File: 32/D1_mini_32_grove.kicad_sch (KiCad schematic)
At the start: 3 parts, among them J1 Conn_01x04_Pin, J2 Conn_01x04_Pin, U1 esp32-wemos-d1-mini

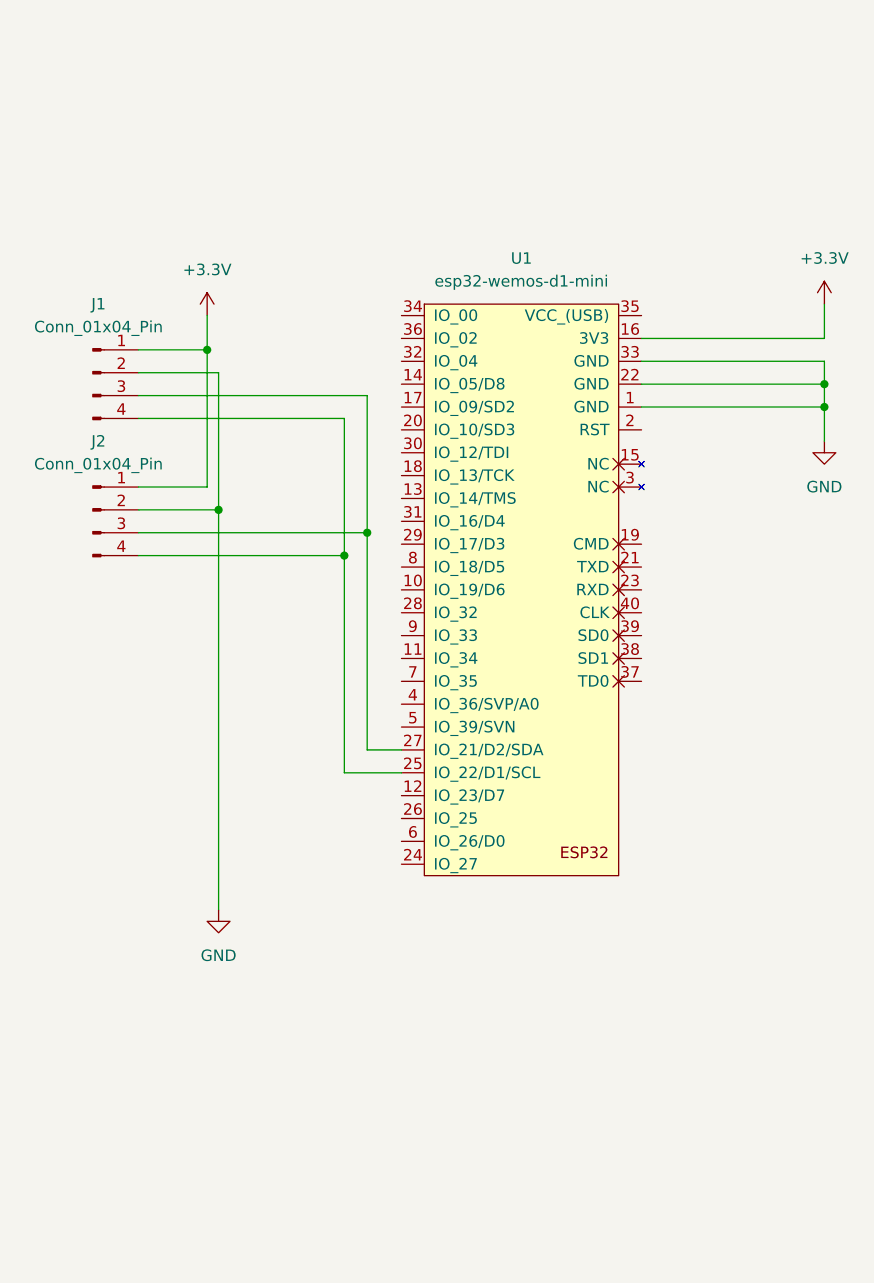
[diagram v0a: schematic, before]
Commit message: First draft of 32 board ready for testrun
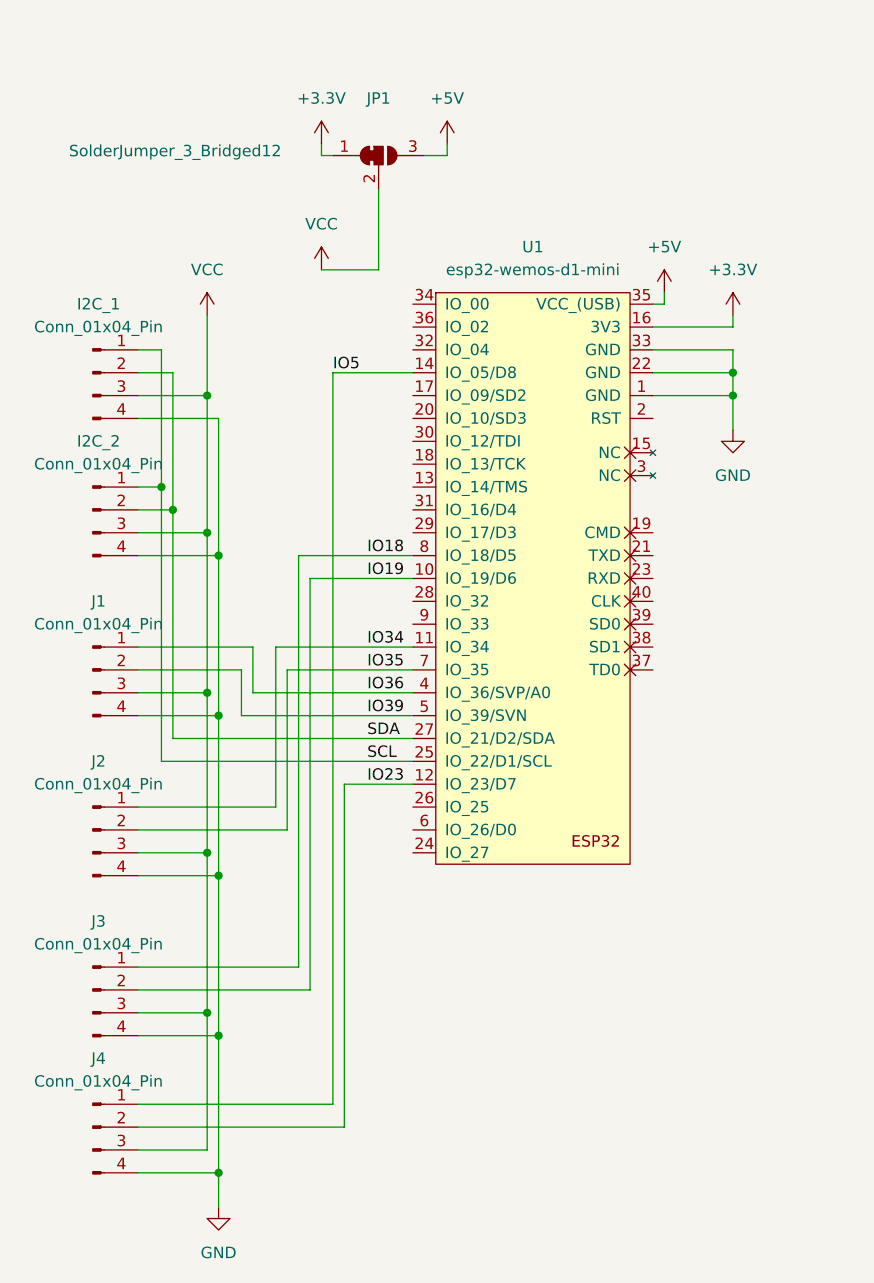
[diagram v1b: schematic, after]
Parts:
- added J1, J2, J3, J4: Conn_01x04_Pin, pretty:NS-Tech_Grove_1x04_P2mm_Vertical, symbol Connector:Conn_01x04_Pin
- added JP1: SolderJumper_3_Bridged12, Jumper:SolderJumper-3_P1.3mm_Bridged12_RoundedPad1.0x1.5mm_NumberLabels, symbol Jumper:SolderJumper_3_Bridged12
- renumbered J1 to I2C_1, J2 to I2C_2
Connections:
- net +3.3V: now also JP1.1 (A); no longer I2C_1.1 (Pin_1), I2C_2.1 (Pin_1)
- net GND: now also I2C_1.4 (Pin_4), I2C_2.4 (Pin_4), J1.4 (Pin_4), J2.4 (Pin_4), J3.4 (Pin_4), J4.4 (Pin_4); no longer I2C_1.2 (Pin_2), I2C_2.2 (Pin_2)
- net IO19: now reaches U1.10 (IO_19/D6)
- net IO19: now also J3.2 (Pin_2)
- net IO34: now reaches U1.11 (IO_34)
- net IO34: now also J2.1 (Pin_1)
- net IO23: now reaches U1.12 (IO_23/D7)
- net IO23: now also J4.2 (Pin_2)
- net IO5: now reaches U1.14 (IO_05/D8)
- net IO5: now also J4.1 (Pin_1)
- net VCC: now reaches I2C_1.3 (Pin_3), I2C_2.3 (Pin_3)
- net VCC: now also J1.3 (Pin_3), J2.3 (Pin_3), J3.3 (Pin_3), J4.3 (Pin_3), JP1.2 (C); no longer U1.27 (IO_21/D2/SDA)
- net +5V: now reaches U1.35 (VCC_(USB))
- net +5V: now also JP1.3 (B)
- net IO36: now reaches U1.4 (IO_36/SVP/A0)
- net IO36: now also J1.1 (Pin_1)
- net IO39: now reaches U1.5 (IO_39/SVN)
- net IO39: now also J1.2 (Pin_2)
- net IO35: now reaches U1.7 (IO_35)
- net IO35: now also J2.2 (Pin_2)
- net IO18: now reaches U1.8 (IO_18/D5)
- net IO18: now also J3.1 (Pin_1)
- new net SCL: I2C_1.1 (Pin_1), I2C_2.1 (Pin_1), U1.25 (IO_22/D1/SCL)
- new net SDA: I2C_1.2 (Pin_2), I2C_2.2 (Pin_2), U1.27 (IO_21/D2/SDA)
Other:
- moved on the sheet: U1

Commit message: Added a switch for VCC selector instead of solder bridge.. its tight but itll work
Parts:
- removed JP1: SolderJumper_3_Bridged12, Jumper:SolderJumper-3_P1.3mm_Bridged12_RoundedPad1.0x1.5mm_NumberLabels, symbol Jumper:SolderJumper_3_Bridged12
- added SW1: SW_Wuerth_450301014042, Button_Switch_THT:SW_Slide-03_Wuerth-WS-SLTV_10x2.5x6.4_P2.54mm, symbol Switch:SW_Wuerth_450301014042
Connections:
- net +3.3V: now also SW1.2 (C)
- net +5V: now also SW1.3 (A)
- net VCC: now also SW1.1 (B)
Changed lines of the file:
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@@
 (kicad_sch
-	(version 20231120)
+	(version 20250114)
 	(generator "eeschema")
-	(generator_version "8.0")
+	(generator_version "9.0")
 	(paper "A4")
 	(junction
@@
 	(wire
 		(pts
-			(xy 93.98 44.45) (xy 95.25 44.45)
+			(xy 97.79 35.56) (xy 97.79 38.1)
 		)
 		(stroke
@@
 	(wire
 		(pts
+			(xy 100.33 48.26) (xy 100.33 57.15)
+		)
+		(stroke
+			(width 0)
+			(type default)
+		)
+	)
+	(wire
+		(pts
 			(xy 85.09 106.68) (xy 85.09 101.6)
 		)
@@
 	(wire
 		(pts
+			(xy 102.87 35.56) (xy 102.87 38.1)
+		)
+		(stroke
+			(width 0)
+			(type default)
+		)
+	)
+	(wire
+		(pts
 			(xy 92.71 91.44) (xy 92.71 137.16)
 		)
@@
 	(wire
 		(pts
-			(xy 93.98 43.18) (xy 93.98 44.45)
-		)
-		(stroke
-			(width 0)
-			(type default)
-		)
-	)
-	(wire
-		(pts
 			(xy 130.81 66.04) (xy 139.7 66.04)
 		)
@@
 		(pts
 			(xy 73.66 134.62) (xy 91.44 134.62)
-		)
-		(stroke
-			(width 0)
-			(type default)
-		)
-	)
-	(wire
-		(pts
-			(xy 100.33 57.15) (xy 100.33 48.26)
 		)
 		(stroke
@@
 	(label "SDA"
 		(at 99.06 109.22 0)
-		(fields_autoplaced yes)
 		(effects
 			(font
@@
 	(label "IO23"
 		(at 99.06 114.3 0)
-		(fields_autoplaced yes)
 		(effects
 			(font
@@
 	(label "SCL"
 		(at 99.06 111.76 0)
-		(fields_autoplaced yes)
 		(effects
 			(font
@@
 	(label "IO34"
 		(at 99.06 99.06 0)
-		(fields_autoplaced yes)
 		(effects
 			(font
@@
 	(label "IO18"
 		(at 99.06 88.9 0)
-		(fields_autoplaced yes)
 		(effects
 			(font
@@
 	(label "IO19"
 		(at 99.06 91.44 0)
-		(fields_autoplaced yes)
 		(effects
 			(font
@@
 	(label "IO5"
 		(at 95.25 68.58 0)
-		(fields_autoplaced yes)
 		(effects
 			(font
@@
 	(label "IO39"
 		(at 99.06 106.68 0)
-		(fields_autoplaced yes)
 		(effects
 			(font
@@
 	(label "IO36"
 		(at 99.06 104.14 0)
-		(fields_autoplaced yes)
 		(effects
 			(font
@@
 	(label "IO35"
 		(at 99.06 101.6 0)
-		(fields_autoplaced yes)
 		(effects
 			(font
@@
 	)
 	(symbol
+		(lib_id "Switch:SW_Wuerth_450301014042")
+		(at 100.33 43.18 90)
+		(unit 1)
+		(exclude_from_sim no)
+		(in_bom yes)
+		(on_board yes)
+		(dnp no)
+		(fields_autoplaced yes)
+		(property "Reference" "SW1"
+			(at 105.41 41.9099 90)
+			(effects
+				(font
+					(size 1.27 1.27)
+				)
+				(justify right)
+			)
+		)
+		(property "Value" "SW_Wuerth_450301014042"
+			(at 105.41 44.4499 90)
+			(effects
+				(font
+					(size 1.27 1.27)
+				)
+				(justify right)
+			)
+		)
+		(property "Footprint" "Button_Switch_THT:SW_Slide-03_Wuerth-WS-SLTV_10x2.5x6.4_P2.54mm"
+			(at 110.49 43.18 0)
+			(effects
+				(font
+					(size 1.27 1.27)
+				)
+				(hide yes)
+			)
+		)
+		(property "Datasheet" "https://www.we-online.com/components/products/datasheet/450301014042.pdf"
+			(at 107.95 43.18 0)
+			(effects
+				(font
+					(size 1.27 1.27)
+				)
+				(hide yes)
+			)
+		)
+		(property "Description" "Switch slide, single pole double throw"
+			(at 100.33 43.18 0)
+			(effects
+				(font
+					(size 1.27 1.27)
+				)
+				(hide yes)
+			)
+		)
+		(pin "1"
+		)
+		(pin "3"
+		)
+		(pin "2"
+		)
+		(instances
+			(project ""
+				(path "/a0e550e8-7254-4170-83ce-2dab5837cc92"
+					(reference "SW1")
+					(unit 1)
+				)
+			)
+		)
+	)
+	(symbol
 		(lib_id "power:+3.3V")
 		(at 93.98 57.15 0)
@@
 	)
 	(symbol
-		(lib_id "Jumper:SolderJumper_3_Bridged12")
-		(at 100.33 44.45 0)
-		(unit 1)
-		(exclude_from_sim yes)
-		(in_bom no)
-		(on_board yes)
-		(dnp no)
-		(property "Reference" "JP1"
-			(at 100.33 38.1 0)
-			(effects
-				(font
-					(size 1.27 1.27)
-				)
-			)
-		)
-		(property "Value" "SolderJumper_3_Bridged12"
-			(at 77.724 43.942 0)
-			(effects
-				(font
-					(size 1.27 1.27)
-				)
-			)
-		)
-		(property "Footprint" "Jumper:SolderJumper-3_P1.3mm_Bridged12_RoundedPad1.0x1.5mm_NumberLabels"
-			(at 100.33 44.45 0)
-			(effects
-				(font
-					(size 1.27 1.27)
-				)
-				(hide yes)
-			)
-		)
-		(property "Datasheet" "~"
-			(at 100.33 44.45 0)
-			(effects
-				(font
-					(size 1.27 1.27)
-				)
-				(hide yes)
-			)
-		)
-		(property "Description" "3-pole Solder Jumper, pins 1+2 closed/bridged"
-			(at 100.33 44.45 0)
-			(effects
-				(font
-					(size 1.27 1.27)
-				)
-				(hide yes)
-			)
-		)
-		(pin "3"
-		)
-		(pin "2"
-		)
-		(pin "1"
-		)
-		(instances
-			(project ""
-				(path "/a0e550e8-7254-4170-83ce-2dab5837cc92"
-					(reference "JP1")
-					(unit 1)
-				)
-			)
-		)
-	)
-	(symbol
 		(lib_id "Connector:Conn_01x04_Pin")
 		(at 68.58 101.6 0)
@@
 	(symbol
 		(lib_id "power:+3.3V")
-		(at 93.98 43.18 0)
+		(at 102.87 35.56 0)
 		(unit 1)
 		(exclude_from_sim no)
@@
 		(on_board yes)
 		(dnp no)
-		(fields_autoplaced yes)
 		(property "Reference" "#PWR03"
-			(at 93.98 46.99 0)
+			(at 102.87 39.37 0)
 			(effects
 				(font
@@
 		)
 		(property "Value" "+3.3V"
-			(at 93.98 38.1 0)
+			(at 102.87 30.48 0)
 			(effects
 				(font
@@
 		)
 		(property "Footprint" ""
-			(at 93.98 43.18 0)
+			(at 102.87 35.56 0)
 			(effects
 				(font
@@
 		)
 		(property "Datasheet" ""
-			(at 93.98 43.18 0)
+			(at 102.87 35.56 0)
 			(effects
 				(font
@@
 		)
 		(property "Description" "Power symbol creates a global label with name \"+3.3V\""
-			(at 93.98 43.18 0)
+			(at 102.87 35.56 0)
 			(effects
 				(font
@@
 	(symbol
 		(lib_id "power:+3.3V")
-		(at 107.95 43.18 0)
+		(at 97.79 35.56 0)
 		(mirror y)
 		(unit 1)
@@
 		(dnp no)
 		(property "Reference" "#PWR08"
-			(at 107.95 46.99 0)
+			(at 97.79 39.37 0)
 			(effects
 				(font
@@
 		)
 		(property "Value" "+5V"
-			(at 107.95 38.1 0)
+			(at 97.79 30.48 0)
 			(effects
 				(font
@@
 		)
 		(property "Footprint" ""
-			(at 107.95 43.18 0)
+			(at 97.79 35.56 0)
 			(effects
 				(font
@@
 		)
 		(property "Datasheet" ""
-			(at 107.95 43.18 0)
+			(at 97.79 35.56 0)
 			(effects
 				(font
@@
 		)
 		(property "Description" "Power symbol creates a global label with name \"+3.3V\""
-			(at 107.95 43.18 0)
+			(at 97.79 35.56 0)
 			(effects
 				(font
@@
 		)
 	)
+	(embedded_fonts no)
 )

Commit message: The 32board had room for one more grove connector... finetuned some 3D stuff too
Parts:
- added J5: Conn_01x04_Pin, pretty:NS-Tech_Grove_1x04_P2mm_Vertical, symbol Connector:Conn_01x04_Pin
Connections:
- net GND: now also J5.4 (Pin_4)
- net VCC: now also J5.3 (Pin_3)
- net at U1.6 (IO_26/D0): now also J5.2 (Pin_2)
- net at U1.9 (IO_33): now also J5.1 (Pin_1)
